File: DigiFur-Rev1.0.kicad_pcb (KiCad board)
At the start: 4 copper layers, 150 x 80 mm, 147 parts, among them J1 705510001, J2 Micro_SD_Card_Det_Hirose_DM3AT, J3 705510001, J4 705510001, J5 Conn_02x09_Odd_Even, J6 Conn_02x06_Odd_Even, Q1 SSM3J327R, SW1 SW_Push, SW2 SW_Push, SW3 SW_Push, SW4 SW_Push, SW5 MX2A-E1NW, U1 TLV840MADL22DBVR, U10 USBLC6-2SC6, U11 MAX98357A, U12 TPS63900, U13 TPS63900, U14 TPS63900, U15 TPS63900, U16 TPS22917DBV, U2 NL17SZ10DBVT, U3 MCP23017x-x-SO, U4 PCF85063AT, U5 ESP32-C6-DevKitC-1, U6 TLV840MADL22DBVR, U7 TPS22917DBV, U8 OPA333 or TLV333 or TLV9041, U9 JLX256128G-931-PL_SPI, Y1 ECS-.327-12.5-34QCS-TR

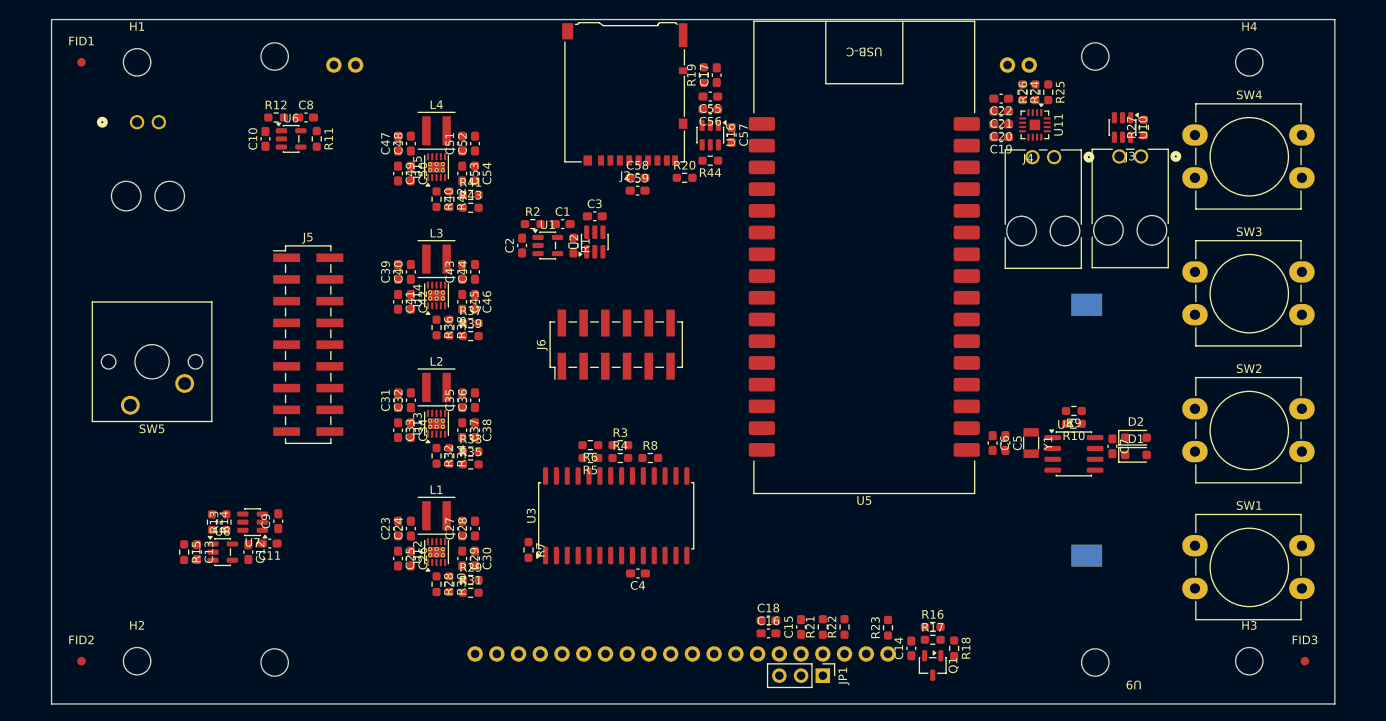
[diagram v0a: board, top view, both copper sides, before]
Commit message: PCB layout done, signal routing finished, power routing remaining.
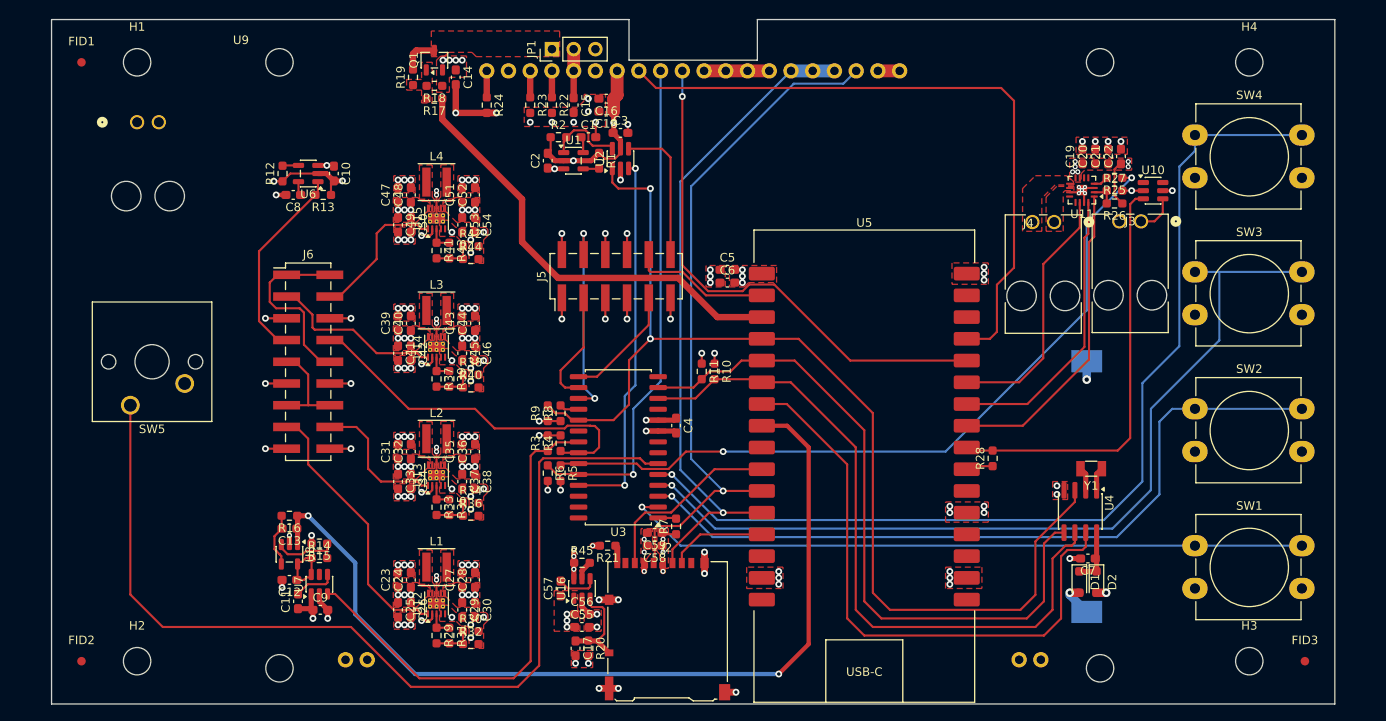
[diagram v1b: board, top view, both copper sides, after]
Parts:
- added R9: 330k, Resistor_SMD:R_0603_1608Metric_Pad0.98x0.95mm_HandSolder, F.Cu at (108.0, 96.0)
- moved U9 128.1 mm to (72.1, 52.9), turned to 0 degrees
- moved R19 92.0 mm to (92.2, 56.8), turned to 90 degrees
- moved Q1 91.6 mm to (94.8, 54.8), turned to 90 degrees
- moved R18 87.1 mm to (94.8, 57.8), turned to 180 degrees
- moved C14 85.4 mm to (97.2, 56.8), turned to -90 degrees
- moved R17 84.9 mm to (94.8, 59.2), turned to 180 degrees
- moved JP1 79.8 mm to (108.5, 53.5), turned to 90 degrees
- moved R24 77.0 mm to (100.9, 60.0), turned to -90 degrees
- moved R23 71.2 mm to (106.0, 60.0), turned to -90 degrees
- moved C17 69.0 mm to (111.2, 123.5), turned to -90 degrees
- moved R22 68.7 mm to (108.5, 60.0), turned to -90 degrees
- moved R20 68.3 mm to (112.8, 123.5), turned to -90 degrees
- moved C15 66.5 mm to (111.0, 60.0), turned to -90 degrees
- moved C16 65.3 mm to (114.8, 59.2), turned to 180 degrees
- moved C55 63.8 mm to (112.0, 121.0), turned to 0 degrees
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- renumbered J6 to J5, J5 to J6, R9 to R10, R10 to R11, R11 to R12, R12 to R13, R13 to R14, R14 to R15, R15 to R16, R16 to R17, R17 to R18, R18 to R19, R19 to R20, R20 to R21, R21 to R22, R22 to R23, R23 to R24, R24 to R25, R25 to R26, R26 to R27, R27 to R28, R28 to R29, R29 to R30, R30 to R31, R31 to R32, R32 to R33, R33 to R34, R34 to R35, R35 to R36, R36 to R37, R37 to R38, R38 to R39, R39 to R40, R40 to R41, R41 to R42, R42 to R43, R43 to R44, R44 to R45
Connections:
- U10 pad 1: ACOM_OD -> unconnected-(U10-I/O1-Pad1)
- U10 pad 3: unconnected-(U10-I/O2-Pad3) -> ACOM_OD
- U10 pad 4: unconnected-(U10-I/O2-Pad4) -> Net-(J3-Pin_1)
- U10 pad 6: Net-(J3-Pin_1) -> unconnected-(U10-I/O1-Pad6)
- U5 pad 10: I2S_DATA -> SPI_MISO
- U5 pad 11: I2S_BCLK -> SPI_CLK
- U5 pad 12: I2S_LRCK -> SPI_MOSI
- U5 pad 13: /MCU/~{INT} -> SPI_~{CS}_SD
- U5 pad 23: SPI_MISO -> ACOM_PU
- U5 pad 24: SPI_CLK -> ACOM_OD
- U5 pad 25: SPI_MOSI -> I2S_DATA
- U5 pad 26: SPI_~{CS}_SD -> I2S_BCLK
- U5 pad 27: SPI_~{CS}_LCD -> I2S_LRCK
- U5 pad 28: LCD_D/~{C} -> SPI_~{CS}_LCD
- U5 pad 29: LCD_LEDA_PWM -> LCD_D/~{C}
- U5 pad 3: ACOM_OD -> LCD_LEDA_PWM
- U5 pad 4: ACOM_PU -> /MCU/~{INT}
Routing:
- net /MCU/~{INT}: track 0.00 -> 128.9 mm, vias 0 -> 2
- net Net-(U3-GPB4): track 0.00 -> 116.2 mm, vias 0 -> 1
- net Net-(U3-GPB5): track 0.00 -> 113.5 mm
- net BAT_MON_ADC: track 0.00 -> 105.3 mm, vias 0 -> 2
- net Net-(U3-GPB3): track 0.00 -> 102.9 mm, vias 0 -> 1
- net Net-(U3-GPB2): track 0.00 -> 88.4 mm, vias 0 -> 1
- net SPK_EN: track 0.00 -> 88.3 mm, vias 0 -> 2
- net GND: track 0.00 -> 83.0 mm, vias 0 -> 132
- net /MCU/I2C_SCL: track 0.00 -> 81.5 mm
- net /MCU/I2C_SDA: track 0.00 -> 81.1 mm
- net Net-(U3-GPB1): track 0.00 -> 80.9 mm, vias 0 -> 1
- net SPI_CLK: track 0.00 -> 80.5 mm, vias 0 -> 1
- net SPI_MOSI: track 0.00 -> 78.0 mm, vias 0 -> 1
- net LCD_D/~{C}: track 0.00 -> 77.0 mm
- net /MCU/MCU_SLOW_CLK: track 0.00 -> 69.8 mm
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- added copper zone on F.Cu, net +3.3V_MCU
- added copper zone on In2.Cu, net +3.3V_MCU
- added copper zone on F.Cu, net +3.3V_PERIPH
- added copper zone on In2.Cu, net +3.3V_PERIPH
- added copper zone on F.Cu, net +3.3V_SD
- added copper zone on F.Cu, net GND
- added copper zone on F.Cu, net Net-(J4-Pin_1)
- added copper zone on F.Cu, net Net-(J4-Pin_2)
- added copper zone on F.Cu, net Net-(JP1-A)
- added copper zone on F.Cu, net Net-(Q1-G)
- added copper zone on F.Cu, net Net-(U12-LX1)
- added copper zone on F.Cu, net Net-(U12-LX2)
- added copper zone on F.Cu, net Net-(U13-LX1)
- added copper zone on F.Cu, net Net-(U13-LX2)
- added copper zone on F.Cu, net Net-(U14-LX1)
- added copper zone on F.Cu, net Net-(U14-LX2)
- added copper zone on F.Cu, net Net-(U15-LX1)
- added copper zone on F.Cu, net Net-(U15-LX2)
- added copper zone on F.Cu, net VBAT
- added copper zone on In2.Cu, net VBAT
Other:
- outline, holes or cut-outs redrawn

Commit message: Routing completed, silkscreen not yet done.
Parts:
- moved C11 1.81 mm to (77.0, 118.0)
- moved C12 1.81 mm to (76.0, 115.5)
- moved C13 1.81 mm to (76.0, 109.5)
- moved C9 1.81 mm to (79.6, 119.0)
- moved R14 1.81 mm to (79.5, 113.0)
- moved R15 1.81 mm to (79.5, 111.2)
- moved R16 1.81 mm to (76.0, 108.0)
- moved U7 1.81 mm to (79.5, 116.0)
- moved U8 1.81 mm to (76.0, 112.5)
- moved C16 1.00 mm to (114.8, 60.2)
- moved C18 1.00 mm to (114.8, 61.8)
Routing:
- net +3.3V_MCU: track 52.6 -> 172.6 mm, vias 21 -> 35
- net +3.3V_PERIPH: track 6.23 -> 86.1 mm, vias 20 -> 27
- net VBAT: track 41.9 -> 50.7 mm
- net BAT_MON_ADC: track 105.3 -> 112.4 mm
- net BAT_MON_EN: track 58.9 -> 60.7 mm
- net GND: track 83.0 -> 84.5 mm, vias 132 -> 131
- added copper zone on B.Cu, net +3.3V_MCU
- added copper zone on B.Cu, net +3.3V_PERIPH
- added copper zone on B.Cu, net +3.3V_SD
- added copper zone on In2.Cu, net GND

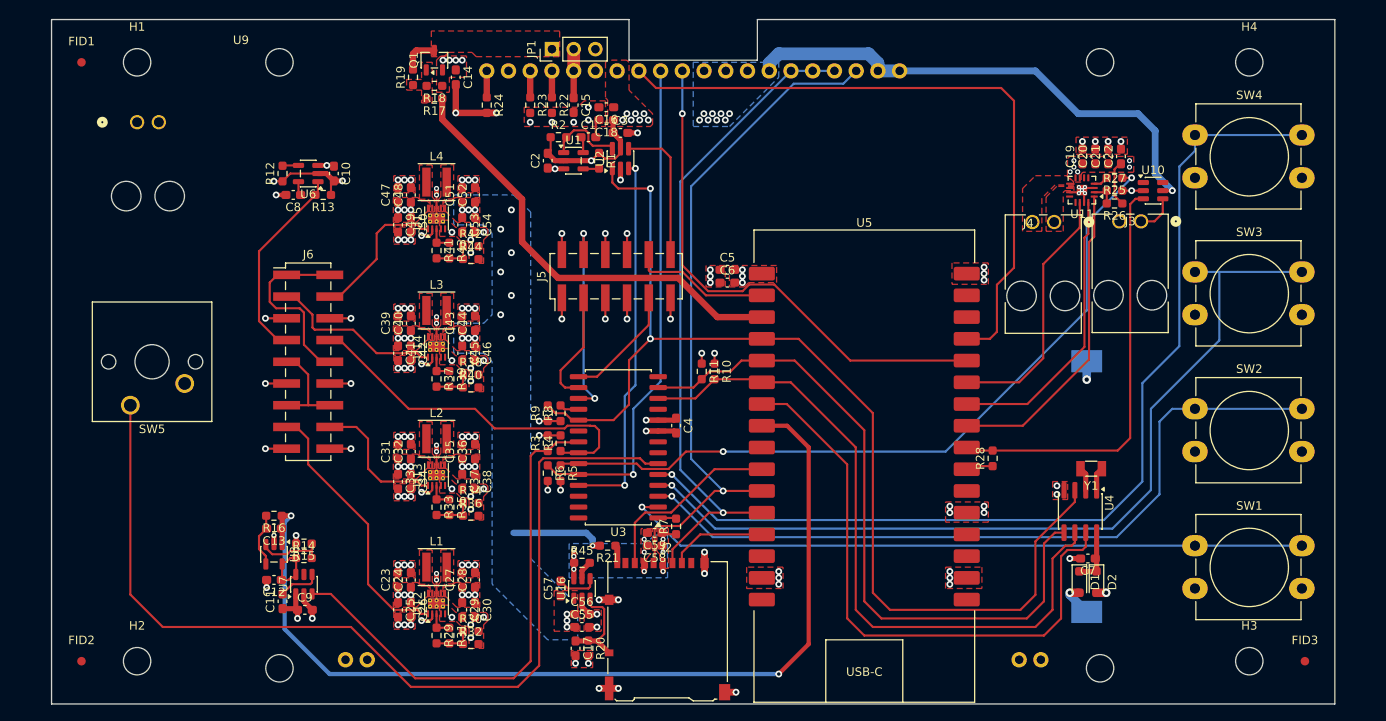
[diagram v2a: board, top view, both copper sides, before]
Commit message: Intermediate silkscreen layout.
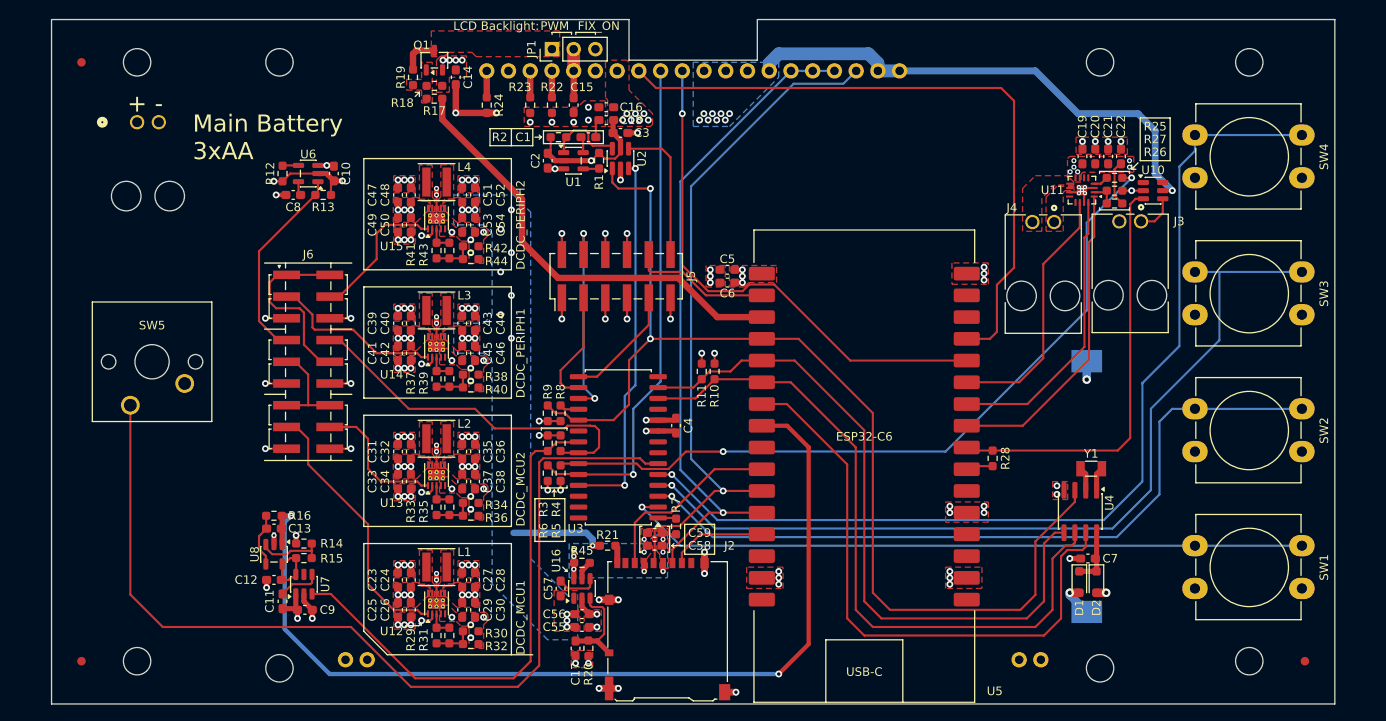
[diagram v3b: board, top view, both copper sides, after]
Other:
- board text added: "+"
- board text added: "-"
- board text added: "BT1 X:121.00 Y:54.59"
- board text added: "DCDC_MCU1"
- board text added: "DCDC_MCU2"
- board text added: "DCDC_PERIPH1"
- board text added: "DCDC_PERIPH2"
- board text added: "ESP32-C6"
- board text added: "FIX_ON"
- board text added: "H1- X:10.00 Y:5.00"
- board text added: "H2- X:10.00 Y:75.00"
- board text added: "H3- X:140.00 Y:75.00"
- board text added: "H4- X:140.00 Y:5.00"
- board text added: "J1-1 X:10.00 Y:12.00"
- board text added: "J2 X:72.00 Y:71.25"
- board text added: "J3-2 X:124.81 Y:23.59"
- board text added: "J4-2 X:114.65 Y:23.67"
- board text added: "LCD Backlight:"
- board text added: "Main Battery 3xAA"
- board text added: "PWM"
- board text added: "RTC Battery 1xCR2032"
- board text added: "SW1-1 X:133.65 Y:61.50"
- board text added: "SW1-1 X:146.15 Y:61.50"
- board text added: "SW1-2 X:133.65 Y:66.50"
- board text added: "SW1-2 X:146.15 Y:66.50"
- board text added: "SW2-1 X:133.65 Y:45.50"
- board text added: "SW2-1 X:146.15 Y:45.50"
- board text added: "SW2-2 X:133.65 Y:50.50"
- board text added: "SW2-2 X:146.15 Y:50.50"
- board text added: "SW3-1 X:133.65 Y:29.50"
- board text added: "SW3-1 X:146.15 Y:29.50"
- board text added: "SW3-2 X:133.65 Y:34.50"
- board text added: "SW3-2 X:146.15 Y:34.50"
- board text added: "SW4-1 X:133.65 Y:13.50"
- board text added: "SW4-1 X:146.15 Y:13.50"
- board text added: "SW4-2 X:133.65 Y:18.50"
- board text added: "SW4-2 X:146.15 Y:18.50"
- board text added: "SW5- X:11.75 Y:40.00"
- board text added: "SW5-1 X:9.21 Y:45.08"
- board text added: "SW5-2 X:15.56 Y:42.54"
- board text added: "U5 X:95.00 Y:48.75"
- board text added: "U9- X:122.56 Y:5.00"
- board text added: "U9- X:122.56 Y:75.83"
- board text added: "U9- X:26.64 Y:5.00"
- board text added: "U9- X:26.64 Y:75.83"
- board text added: "[ GRID ORIGIN ]"

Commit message: Finished silkscreen. Need to add ground stitching via before sending to fab.
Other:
- board text added: "AUTO"
- board text added: "EN"
- board text added: "MCU DCDC 1"
- board text added: "MCU DCDC 2"
- board text added: "MCU DCDC MODE"
- board text added: "OFF"
- board text added: "ON"
- board text added: "PERIPH DCDC 1"
- board text added: "PERIPH DCDC 2"
- board text added: "PERIPH DCDC MODE"

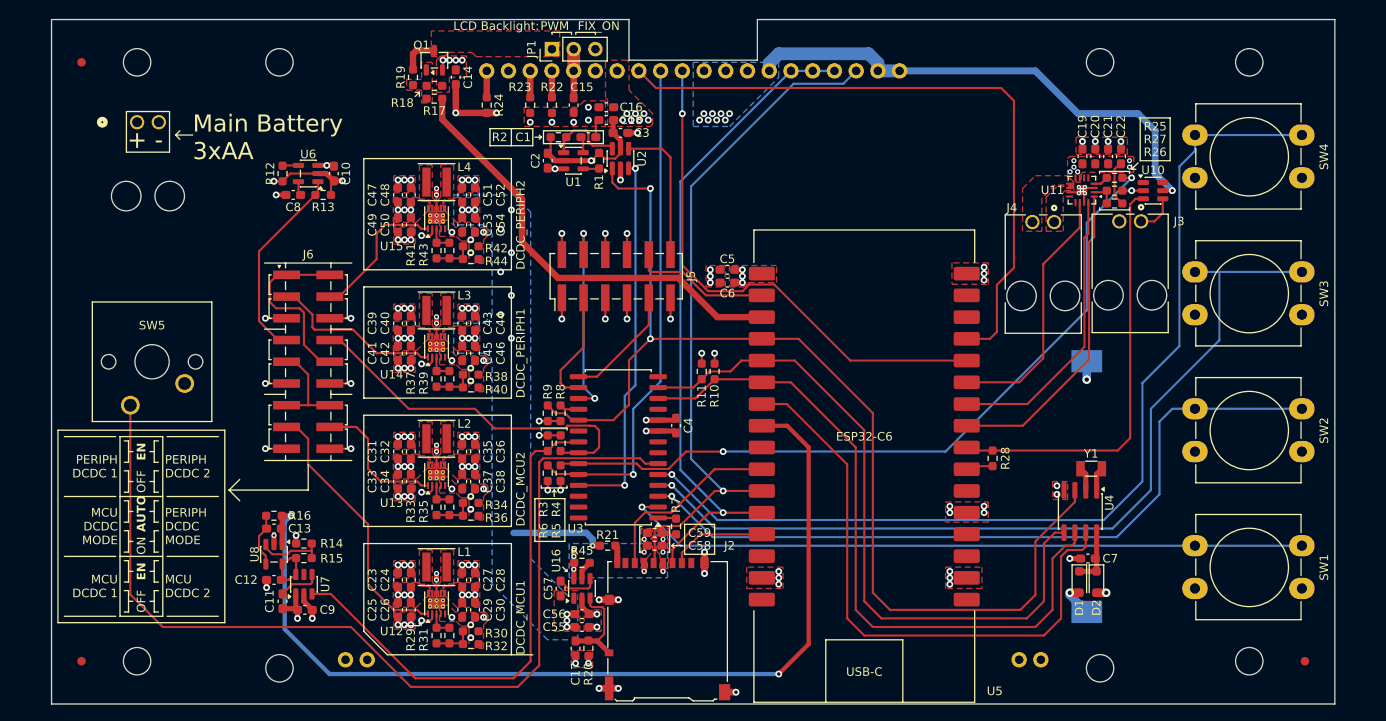
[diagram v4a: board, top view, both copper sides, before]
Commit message: Updated pairing button.
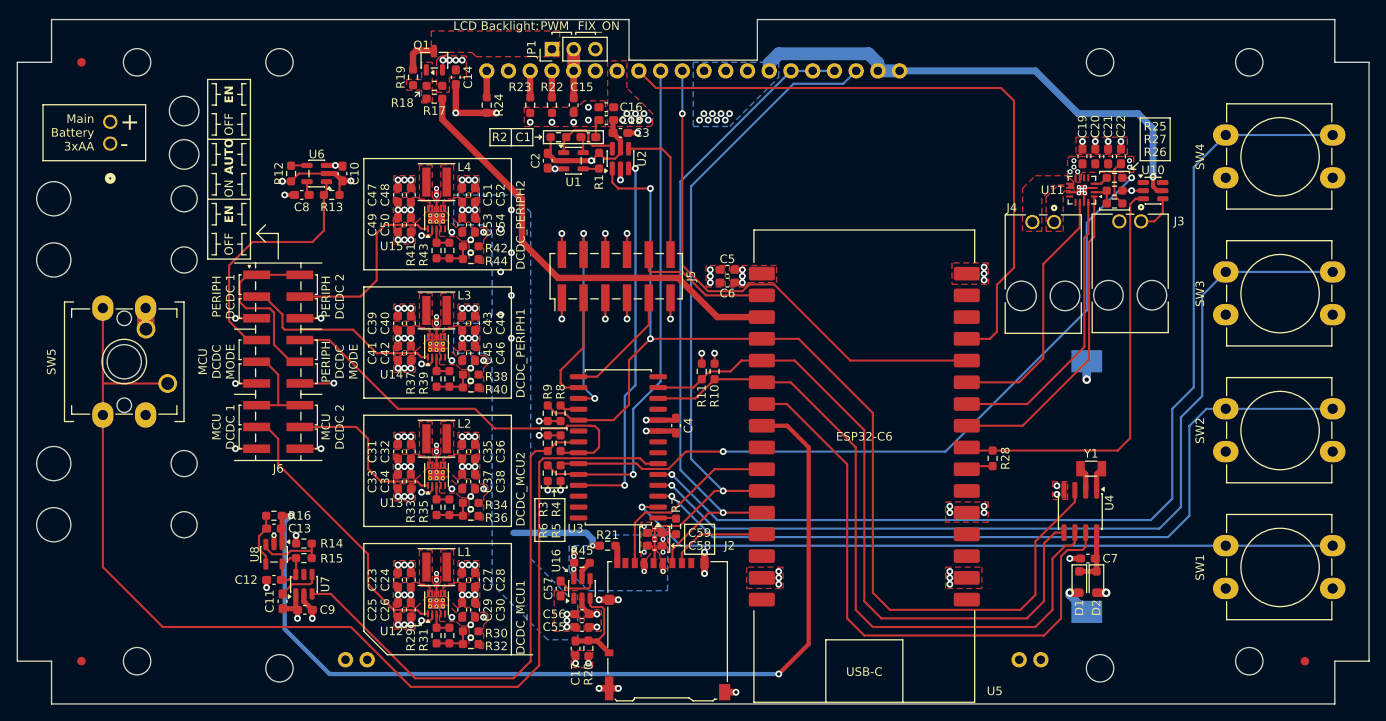
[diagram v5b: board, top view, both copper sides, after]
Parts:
- added SW6: SW_Push, Button_Switch_THT:SW_PUSH-12mm_Wuerth-430476085716, F.Cu at (56.0, 96.2)
- SW5: footprint Button_Switch_Keyboard:SW_Cherry_MX_1.00u_PCB -> Button_Switch_Keyboard:SW_Cherry_MX_2.75u_PCB
- moved SW5 5.05 mm to (63.6, 92.5), turned to -90 degrees
- moved J1 4.01 mm to (56.9, 64.5), turned to -90 degrees
- moved SW1 3.60 mm to (187.2, 111.5)
- moved SW2 3.60 mm to (187.2, 95.5)
- moved SW3 3.60 mm to (187.2, 79.5)
- moved SW4 3.60 mm to (187.2, 63.5)
- moved J6 3.50 mm to (76.5, 90.0)
- moved C10 1.00 mm to (84.0, 68.0)
- moved C8 1.00 mm to (79.2, 70.5)
- moved R12 1.00 mm to (78.0, 68.0)
- moved R13 1.00 mm to (82.8, 70.5)
- moved U6 1.00 mm to (81.0, 68.0)
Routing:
- net Net-(U3-GPB5): track 113.5 -> 133.8 mm
- net GND: track 84.5 -> 94.4 mm
- net PWR_MCU_EN: track 23.3 -> 29.3 mm
- net DCDC_PERIPH2_EN: track 16.9 -> 21.9 mm
- net Net-(U3-GPB2): track 88.4 -> 93.2 mm
- net Net-(U3-GPB4): track 116.2 -> 120.9 mm
- net Net-(U3-GPB1): track 80.9 -> 84.5 mm
- net Net-(U3-GPB3): track 102.9 -> 106.4 mm
- net DCDC_PERIPH1_EN: track 20.3 -> 23.8 mm
- net PWR_PERIPH_EN: track 43.0 -> 46.5 mm
- net DCDC_MCU2_EN: track 16.4 -> 19.9 mm
- net VBAT: track 50.7 -> 53.8 mm
- net DCDC_MCU1_EN: track 31.4 -> 32.9 mm
- net +3.3V_MCU: track 172.6 -> 171.4 mm
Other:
- board size 150 x 80 mm -> 158 x 80 mm
- board text removed: "J1-1 X:10.00 Y:12.00"
- board text removed: "SW5- X:11.75 Y:40.00"
- board text removed: "SW5-1 X:9.21 Y:45.08"
- board text removed: "SW5-2 X:15.56 Y:42.54"

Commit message: Final PCB for 1.0.
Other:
- board text added: "1 0 GPIO EXP A0"
- board text added: "1 0 GPIO EXP A1"
- board text added: "A2 GPIO EXP 1 0"
- board text added: "MCU EN ON AUTO"
